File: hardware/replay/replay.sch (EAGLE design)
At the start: 25 parts, among them J1 SQUALL_HEADER, J3 PJ-102AH, SW1 OS103011, SW2 500ASSP, U1 LT3083, U2 LT3083

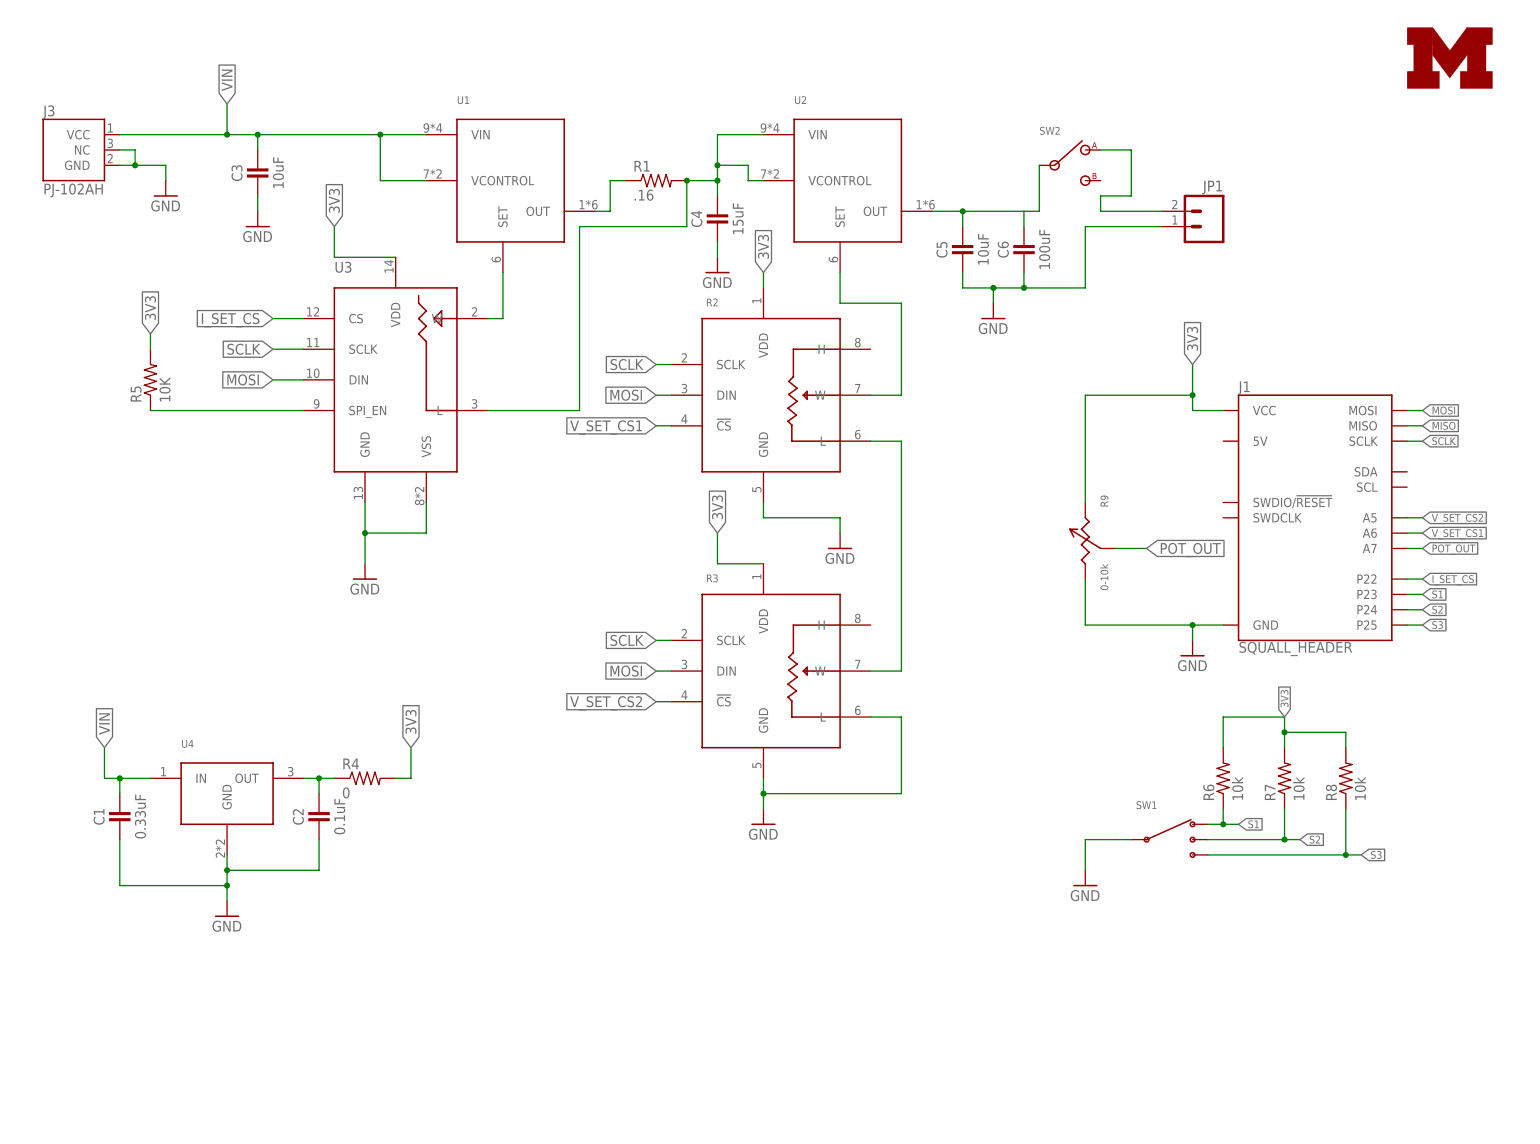
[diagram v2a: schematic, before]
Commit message: cleaned up schematic and changed screw terminal
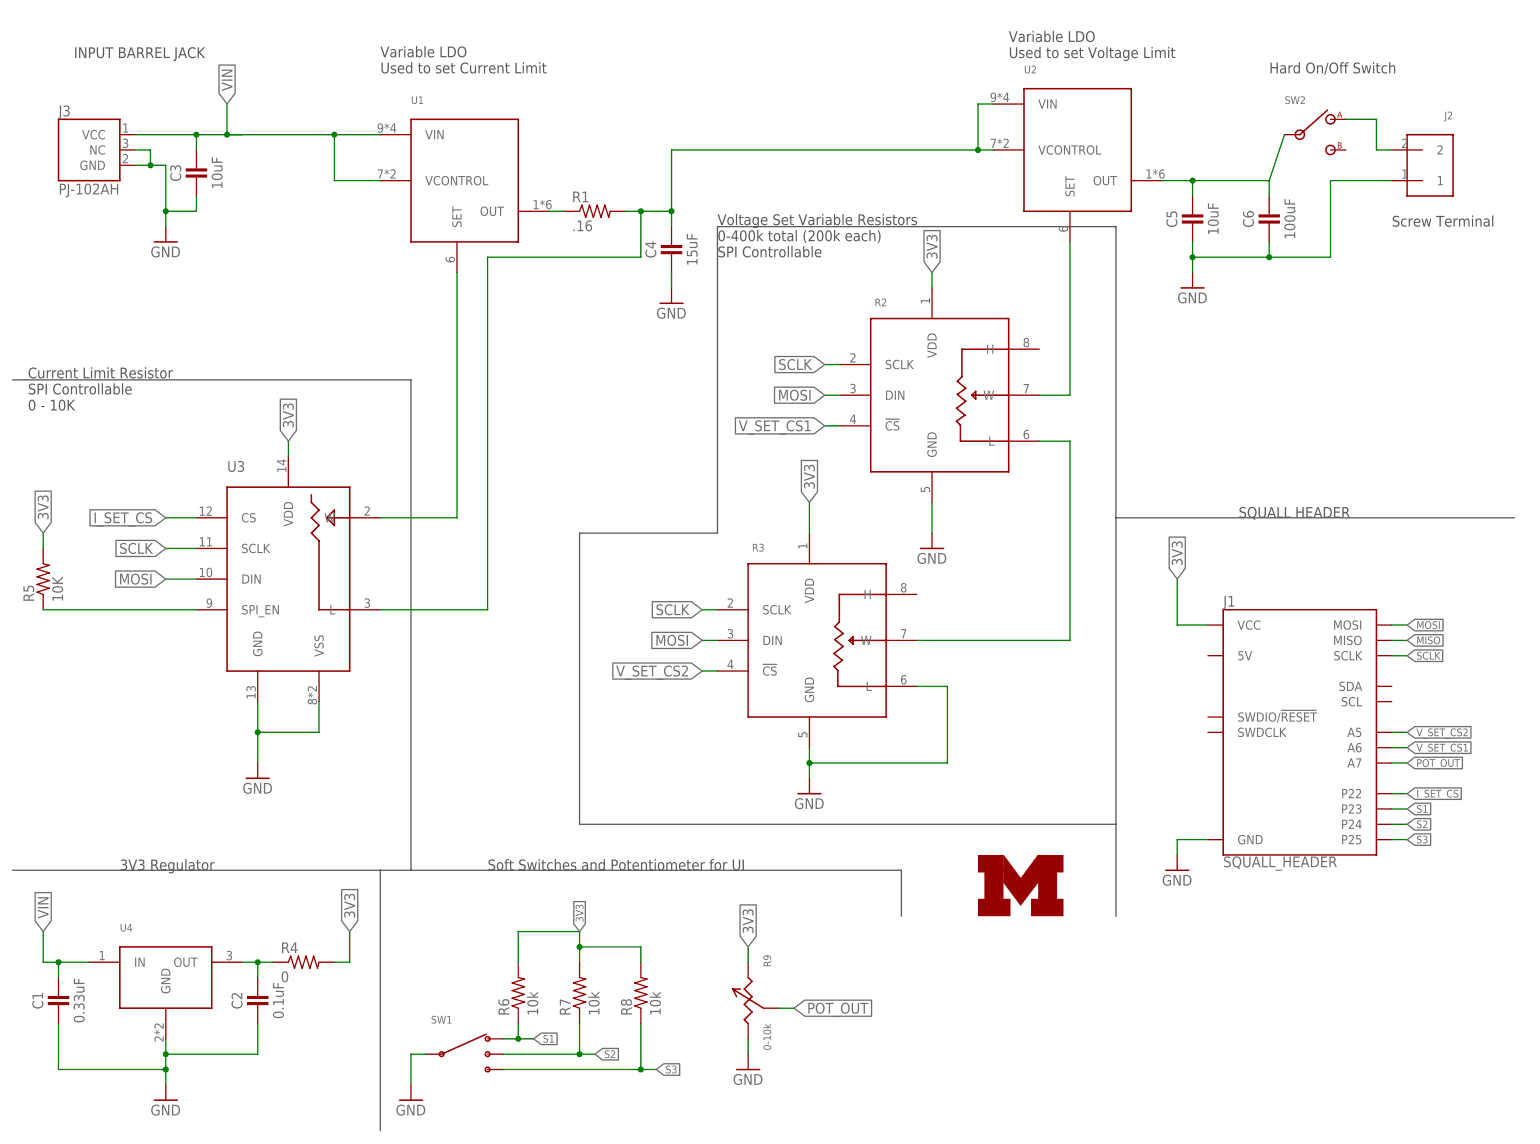
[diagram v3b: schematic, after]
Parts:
- removed JP1: (no value), SparkFun-Connectors:M025MM
- added J2: SCREW_TERMINAL, connector:SCREW_TERMINAL
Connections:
- net GND: now also J2.1; no longer JP1.1
- net OUTS: now also J2.2; no longer JP1.2
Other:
- note added: "3V3 Regulator"
- note added: "Current Limit Resistor SPI Controllable 0 - 10K"
- note added: "Hard On/Off Switch"
- note added: "INPUT BARREL JACK"
- note added: "SQUALL HEADER"
- note added: "Screw Terminal"
- note added: "Soft Switches and Potentiometer for UI"
- note added: "Variable LDO Used to set Current Limit"
- note added: "Variable LDO Used to set Voltage Limit"
- note added: "Voltage Set Variable Resistors 0-400k total (200k each) SPI Controllable"
- moved on the sheet: C1, C2, C3, C4, C5, C6, J1, J3, R1, R2, R3, R4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

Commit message: added the shipped version of replay
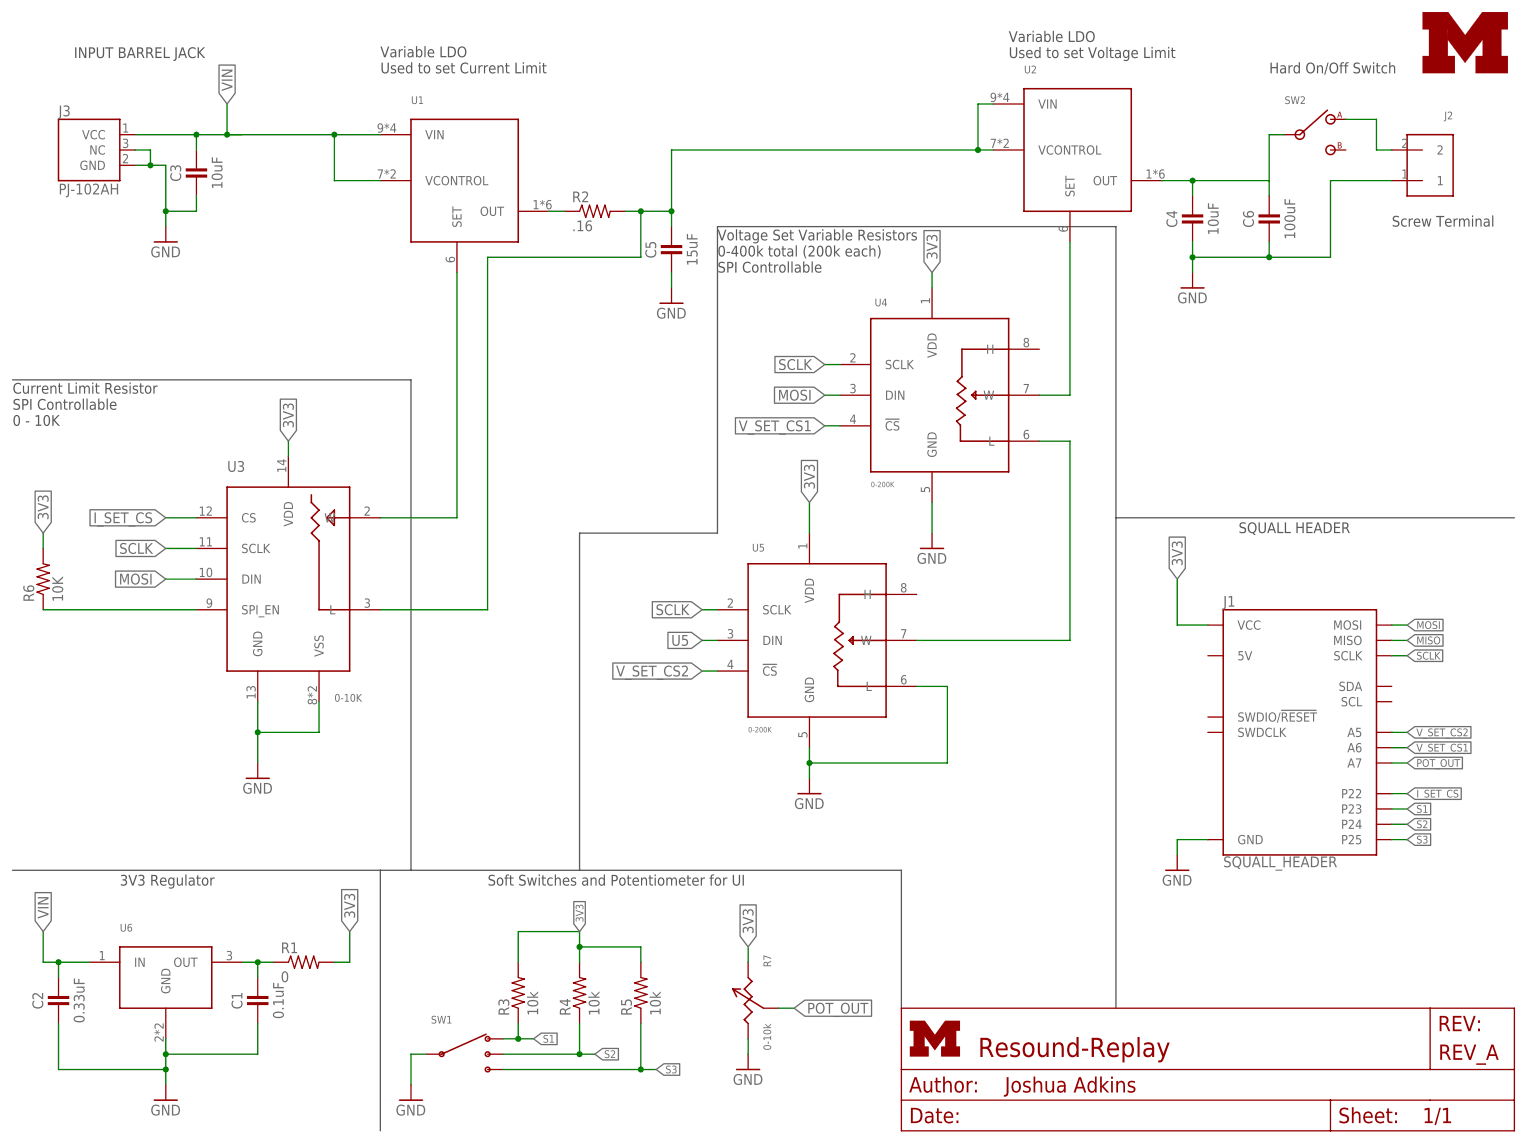
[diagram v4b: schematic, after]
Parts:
- removed R8: 10k, passives:RESISTOR
- removed R9: 0-10k, pots:POT
- added U5: 0-200K, chips:MAX5424
- added U6: (no value), chips:UA78MXX
- C1: value 0.33uF -> 0.1uF
- C2: value 0.1uF -> 0.33uF
- C4: value 15uF -> 10uF
- C5: value 10uF -> 15uF
- R1: value .16 -> 0; device SparkFun-Passives:RESISTOR2512 -> passives:RESISTOR
- R2: value (none) -> .16; device chips:MAX5424 -> SparkFun-Passives:RESISTOR2512
- R3: value (none) -> 10k; device chips:MAX5424 -> passives:RESISTOR
- R4: value 0 -> 10k
- R5: value 10K -> 10k
- R6: value 10k -> 10K
- R7: value 10k -> 0-10k; device passives:RESISTOR -> pots:POT3310C
- U3: value (none) -> 0-10K
- U4: value (none) -> 0-200K; device chips:UA78MXX -> chips:MAX5424
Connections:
- new net U5: U5.DIN
- net 3V3: now also R1.2, R3.2, R7.1, U4.VDD, U5.VDD; no longer R2.VDD, R3.VDD, R7.2, R8.2, R9.1
- net GND: now also R7.3, U5.GND, U5.L, U6.GND; no longer R2.GND, R3.GND, R3.L, R9.3
- net MOSI: now also U4.DIN; no longer R2.DIN, R3.DIN
- net N$5: now also U4.W; no longer R2.W
- net N$6: now also U4.L, U5.W; no longer R2.L, R3.W
- net N$7: now also C1.1, R1.1, U6.OUT; no longer C2.1, R4.1, U4.OUT
- net N$9: now also R6.1; no longer R5.1
- net OUT: now also C4.1; no longer C5.1
- net OUT1: now also R2.1; no longer R1.1
- net POT_OUT: now also R7.2; no longer R9.2
- net S1: now also R3.1; no longer R6.1
- net S2: now also R4.1; no longer R7.1
- net S3: now also R5.1; no longer R8.1
- net SCLK: now also U4.SCLK, U5.SCLK; no longer R2.SCLK, R3.SCLK
- net VIN: now also C2.1, U6.IN; no longer C1.1, U4.IN
- net VIN2: now also C5.1, R2.2; no longer C4.1, R1.2
- net V_SET_CS1: now also U4.!CS; no longer R2.!CS
- net V_SET_CS2: now also U5.!CS; no longer R3.!CS
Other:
- moved on the sheet: C1, C2, C4, C5, R1, R4, R5, R6
